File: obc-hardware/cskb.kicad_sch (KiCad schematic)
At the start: 2 parts, among them J107 Conn_02x26_Odd_Even, J108 Conn_02x26_Odd_Even

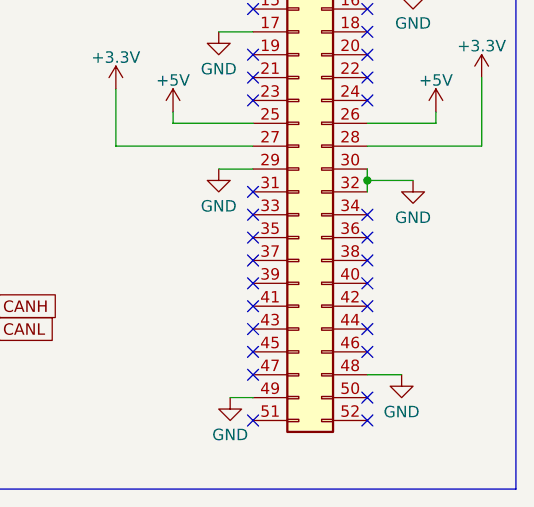
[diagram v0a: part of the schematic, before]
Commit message: added GPIO for payload
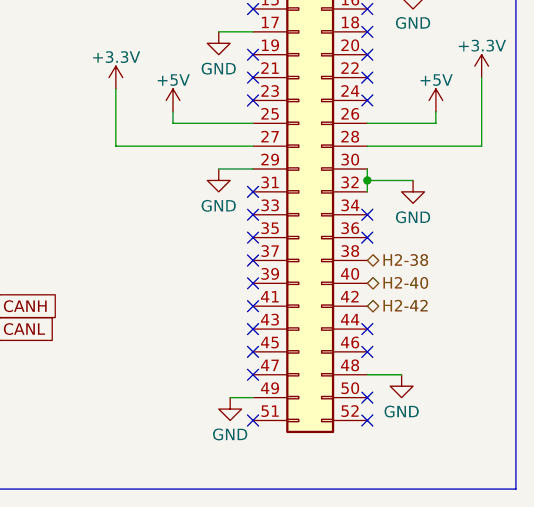
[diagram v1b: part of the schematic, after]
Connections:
- net H2-38: now reaches J108.38 (Pin_38)
- net H2-40: now reaches J108.40 (Pin_40)
- net H2-42: now reaches J108.42 (Pin_42)
- no-connect marks 86 -> 83
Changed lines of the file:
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@@
   (no_connect (at 167.64 76.2))
   (no_connect (at 138.43 124.46))
-  (no_connect (at 180.34 116.84))
   (no_connect (at 180.34 76.2))
   (no_connect (at 167.64 71.12))
   (no_connect (at 138.43 129.54))
   (no_connect (at 138.43 93.98))
-  (no_connect (at 180.34 114.3))
   (no_connect (at 125.73 78.74))
   (no_connect (at 138.43 73.66))
@@
   (no_connect (at 167.64 111.76))
   (no_connect (at 125.73 88.9))
-  (no_connect (at 180.34 119.38))
   (no_connect (at 138.43 86.36))
   (wire (pts (xy 180.34 99.06) (xy 187.96 99.06))
@@
     )
   )
+  (hierarchical_label "H2-40" (shape bidirectional) (at 180.34 116.84 0) (fields_autoplaced)
+    (effects (font (size 1.27 1.27)) (justify left))
+  )
+  (hierarchical_label "H2-42" (shape bidirectional) (at 180.34 119.38 0) (fields_autoplaced)
+    (effects (font (size 1.27 1.27)) (justify left))
+  )
+  (hierarchical_label "H2-38" (shape bidirectional) (at 180.34 114.3 0) (fields_autoplaced)
+    (effects (font (size 1.27 1.27)) (justify left))
+  )
   (symbol (lib_id "power:GND") (at 162.56 78.74 0) (unit 1)
